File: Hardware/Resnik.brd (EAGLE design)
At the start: 64.8 x 100 mm, 188 parts, among them IC1 ATMEGA644M, J1 CONN_82.54_SCREW, J3 CONN_42.54_SCREW, J4 CONN_82.54_SCREW, Q1 DMG3404, Q2 DMG3404, Q3 FDN360P, Q4 FDN360P, Q5 FDN360P, Q6 DMG3404, U1 TLV61220DBV, U10 TPS22917DBV, U11 SN74AUP1G04YFP, U12 SN74AUP1G04YFP, U13 SN74AUP2G86SOT833-1, U14 SN74AUP2G08DQE, U15 SN74AUP2G08DQE, U16 SN74AUP2G08DQE, U17 MIC2544MSOP, U18 MIC2544MSOP, U19 MIC2544MSOP, U2 TPS62822DLC, U20 MIC2544MSOP, U21 TPS22917DBV, U22 TPS22917DBV, U23 FT231X-Q, U24 SN74LVC1G3157DRL, U25 SN74AUP3G34DCU, U26 TXS0102DQM, U27 TXS0108RGY, U28 TXS0108RGY, U29 TXS0104RGY, U3 TPS61032RSA, U30 MCP4726A2SOT-23, U31 BME280, U32 ADS1115, U33 ADS1115, U34 INA211DCK, U35 INA210DCK, U36 TCA9555RTW, U5 BQ2980RUG, U6 TPS2105, U7 LTC4412S6, U8 TPL5111DDC, U9 TPS79733

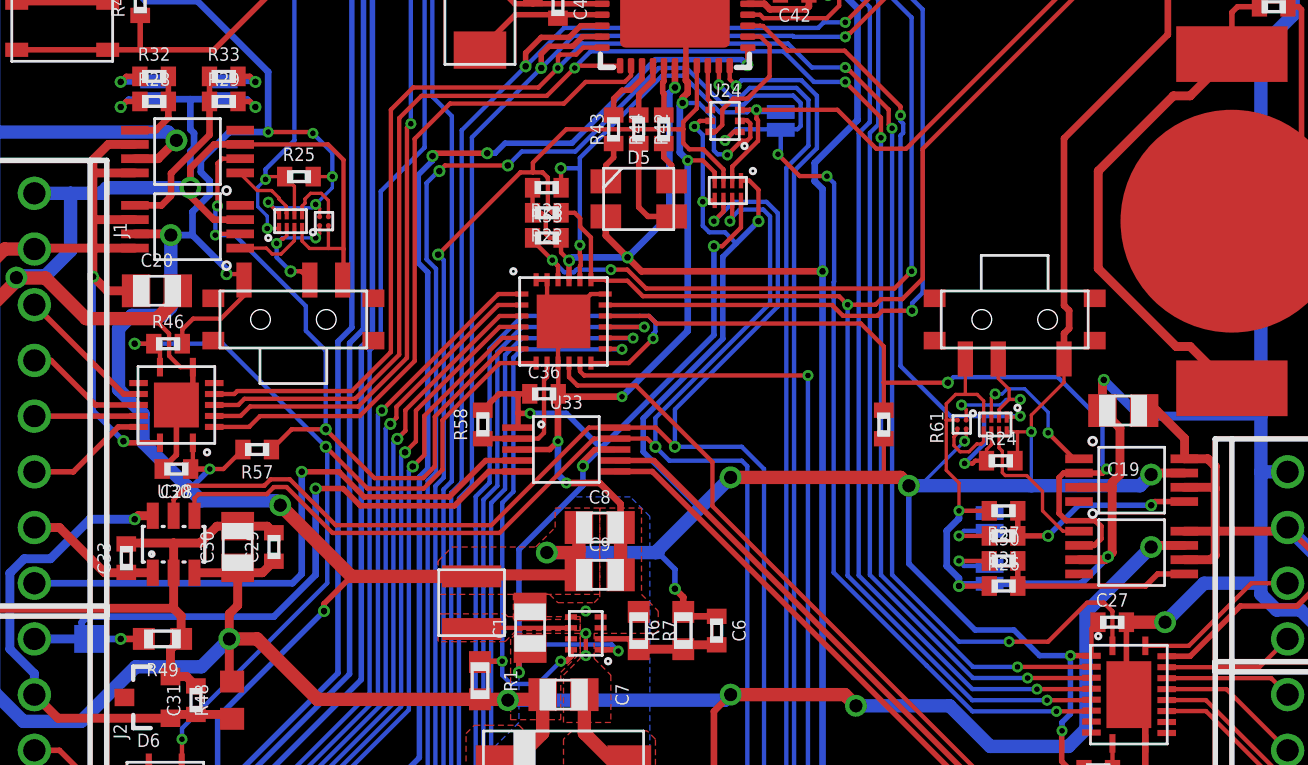
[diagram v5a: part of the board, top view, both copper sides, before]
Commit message: Added dimensions, updated part numbers
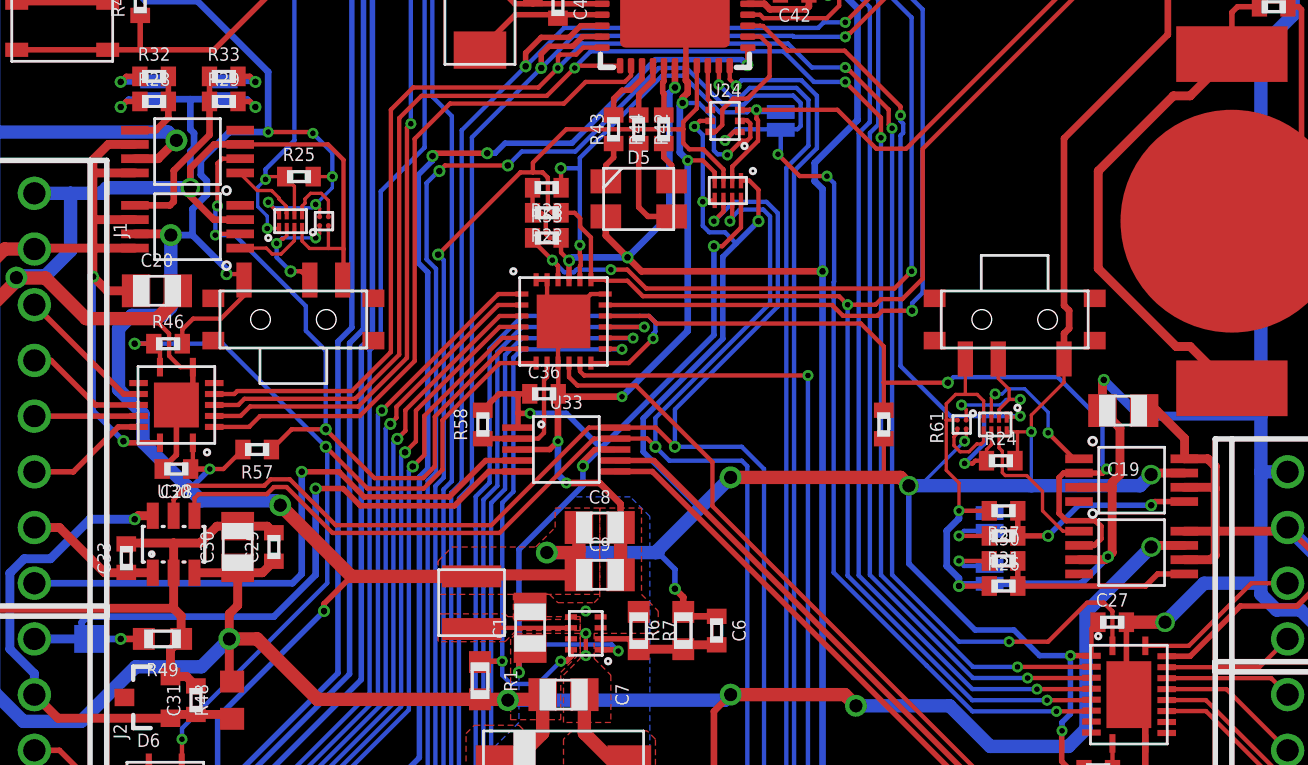
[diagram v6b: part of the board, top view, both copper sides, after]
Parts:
- moved U$4 5.08 mm to (15.1, 64.5)
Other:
- board text added: "Project Resnik v0.0 ---------------- Developed by Northern Widget and University of Minnesota"
- board text removed: "Project Resnik v0.1 ---------------- Developed by Northern Widget and University of Minnesota"

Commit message: Fixed part value for TCA9555 (to TCA9535)
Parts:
- U36: value TCA9555RTW -> TCA9535RTW
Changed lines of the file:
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@@
 <attribute name="VALUE" x="12.192" y="5.334" size="0.6096" layer="27" font="vector" ratio="20" rot="R90" align="top-center"/>
 </element>
-<element name="U36" library="bschulz" package="RTW_S-PWQFN-N24" value="TCA9555RTW" x="27.94" y="52.578" smashed="yes">
-<attribute name="DIGIKEY" value="296-24857-1-ND" x="27.94" y="52.578" size="0.8128" layer="27" font="vector" ratio="15" display="off"/>
+<element name="U36" library="bschulz" package="RTW_S-PWQFN-N24" value="TCA9535RTW" x="27.94" y="52.578" smashed="yes">
+<attribute name="DIGIKEY" value="296-25156-1-ND" x="27.94" y="52.578" size="0.8128" layer="27" font="vector" ratio="15" display="off"/>
+<attribute name="DISP" value="TCA9535" x="27.94" y="52.578" size="1.778" layer="27" display="off"/>
 <attribute name="MF" value="TI" x="27.94" y="52.578" size="0.8128" layer="27" font="vector" ratio="15" display="off"/>
-<attribute name="MPN" value="TCA9555RTWR" x="27.94" y="52.578" size="0.8128" layer="27" font="vector" ratio="15" display="off"/>
+<attribute name="MPN" value="TCA9535RTWR" x="27.94" y="52.578" size="0.8128" layer="27" font="vector" ratio="15" display="off"/>
 </element>
 <element name="C28" library="bschulz_passives" package="C0402" value="0.1uF" x="10.287" y="45.847" smashed="yes" rot="R180">

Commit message: Fixed MPPT set resistors
Fixed the order of the MPPT voltage set resistors. Correct values were used, but in the wrong orientation, this has been corrected
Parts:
- R13: value 91k -> 182k
- R16: value 182k -> 91k
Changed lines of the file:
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@@
 <attribute name="VALUE" x="25.019" y="0.635" size="0.6096" layer="27" font="vector" ratio="15" align="center"/>
 </element>
-<element name="R13" library="bschulz_passives" package="R0603" value="91k" x="28.829" y="6.35" smashed="yes" rot="R180">
-<attribute name="DIGIKEY" value="P91.0KHCT-ND" x="28.829" y="6.35" size="0.8128" layer="27" font="vector" ratio="15" rot="R180" display="off"/>
+<element name="R13" library="bschulz_passives" package="R0603" value="182k" x="28.829" y="6.35" smashed="yes" rot="R180">
+<attribute name="DIGIKEY" value="P182KHCT-ND" x="28.829" y="6.35" size="0.8128" layer="27" font="vector" ratio="15" rot="R180" display="off"/>
 <attribute name="MF" value="Panasonic" x="28.829" y="6.35" size="0.8128" layer="27" font="vector" ratio="15" rot="R180" display="off"/>
-<attribute name="MPN" value="ERJ-3EKF9102V" x="28.829" y="6.35" size="0.8128" layer="27" font="vector" ratio="15" rot="R180" display="off"/>
+<attribute name="MPN" value="ERJ-3EKF1823V" x="28.829" y="6.35" size="0.8128" layer="27" font="vector" ratio="15" rot="R180" display="off"/>
 <attribute name="NAME" x="28.829" y="4.953" size="0.6096" layer="25" font="vector" ratio="15" rot="R180" align="center"/>
 <attribute name="VALUE" x="28.829" y="7.747" size="0.6096" layer="27" font="vector" ratio="15" rot="R180" align="center"/>
-<attribute name="VALUE_PART" value="91k" x="28.829" y="6.35" size="0.8128" layer="27" font="vector" ratio="15" rot="R180" display="off"/>
+<attribute name="VALUE_PART" value="182k" x="28.829" y="6.35" size="0.8128" layer="27" font="vector" ratio="15" rot="R180" display="off"/>
 </element>
-<element name="R16" library="bschulz_passives" package="R0603" value="182k" x="28.829" y="4.318" smashed="yes" rot="R180">
-<attribute name="DIGIKEY" value="P182KHCT-ND" x="28.829" y="4.318" size="0.8128" layer="27" font="vector" ratio="15" rot="R180" display="off"/>
+<element name="R16" library="bschulz_passives" package="R0603" value="91k" x="28.829" y="4.318" smashed="yes" rot="R180">
+<attribute name="DIGIKEY" value="P91.0KHCT-ND" x="28.829" y="4.318" size="0.8128" layer="27" font="vector" ratio="15" rot="R180" display="off"/>
 <attribute name="MF" value="Panasonic" x="28.829" y="4.318" size="0.8128" layer="27" font="vector" ratio="15" rot="R180" display="off"/>
-<attribute name="MPN" value="ERJ-3EKF1823V" x="28.829" y="4.318" size="0.8128" layer="27" font="vector" ratio="15" rot="R180" display="off"/>
+<attribute name="MPN" value="ERJ-3EKF9102V" x="28.829" y="4.318" size="0.8128" layer="27" font="vector" ratio="15" rot="R180" display="off"/>
 <attribute name="NAME" x="28.829" y="2.921" size="0.6096" layer="25" font="vector" ratio="15" rot="R180" align="center"/>
 <attribute name="VALUE" x="28.829" y="5.715" size="0.6096" layer="27" font="vector" ratio="15" rot="R180" align="center"/>
-<attribute name="VALUE_PART" value="182k" x="28.829" y="4.318" size="0.8128" layer="27" font="vector" ratio="15" rot="R180" display="off"/>
+<attribute name="VALUE_PART" value="91k" x="28.829" y="4.318" size="0.8128" layer="27" font="vector" ratio="15" rot="R180" display="off"/>
 </element>
 <element name="R17" library="bschulz_passives" package="R0603" value="330k" x="28.829" y="2.286" smashed="yes">
